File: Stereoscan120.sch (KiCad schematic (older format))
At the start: 0 parts

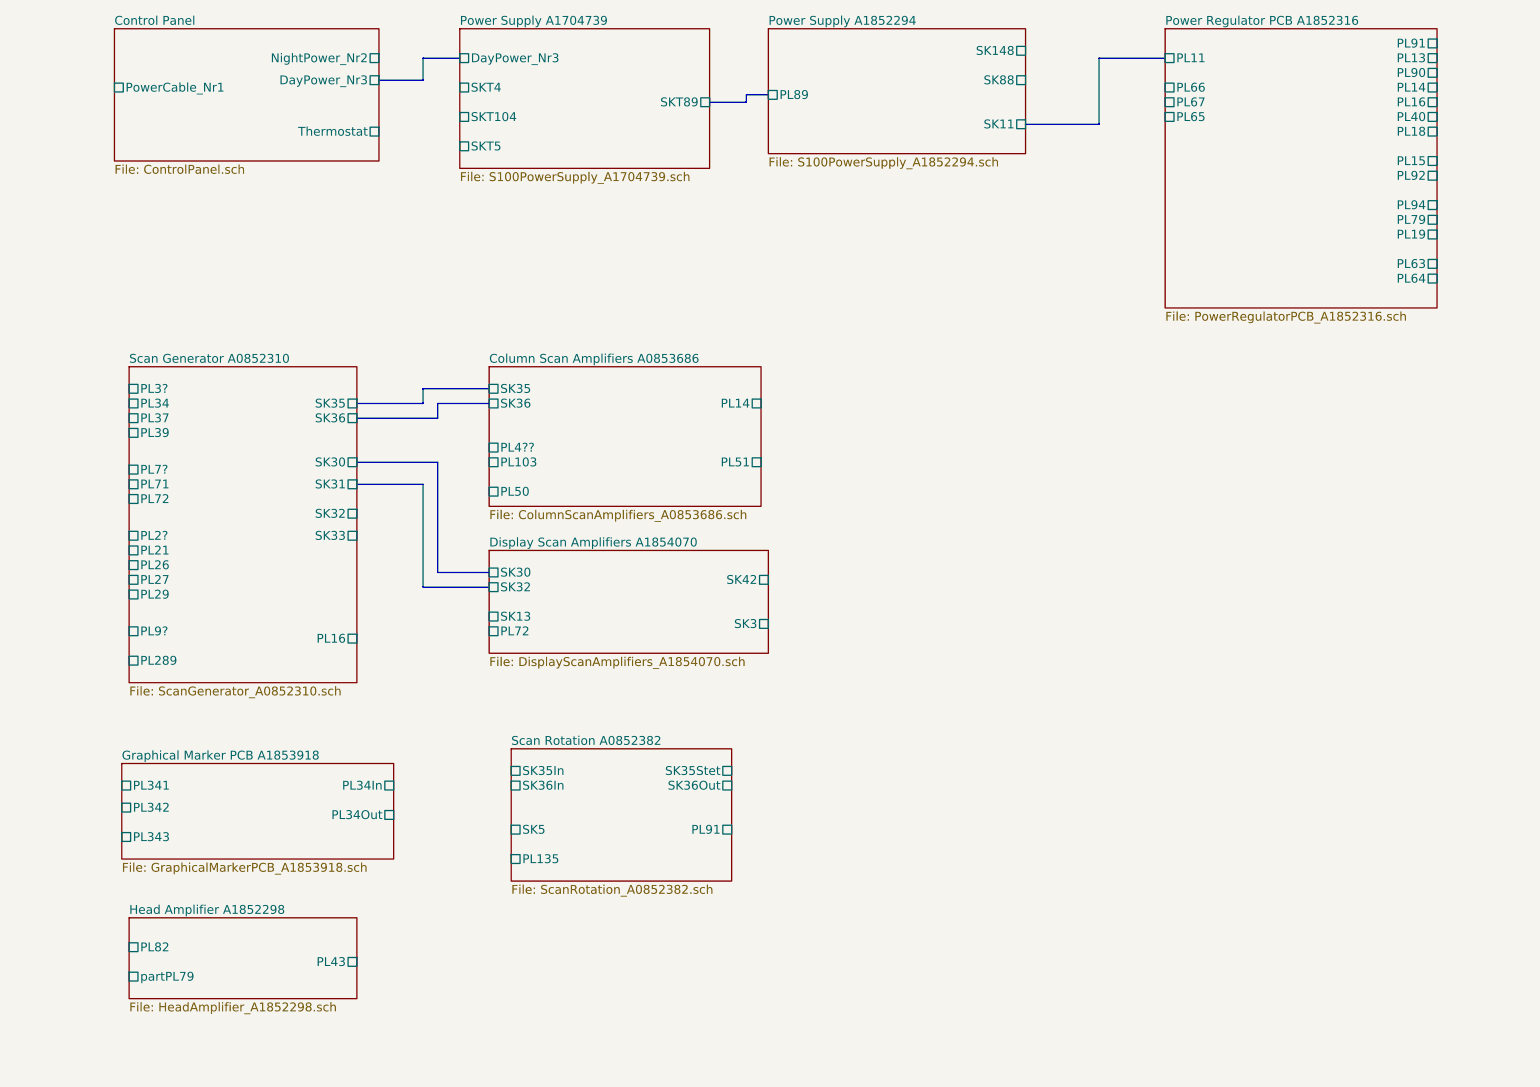
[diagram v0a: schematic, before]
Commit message: Corrects mistakes in existing sub schematics
This corrections were done based on comparison with the actual paper
schematics.
Mainly renaming some pins, which were labled wrongly, plus addid of additional
pins (sockets) which had been overlooked.
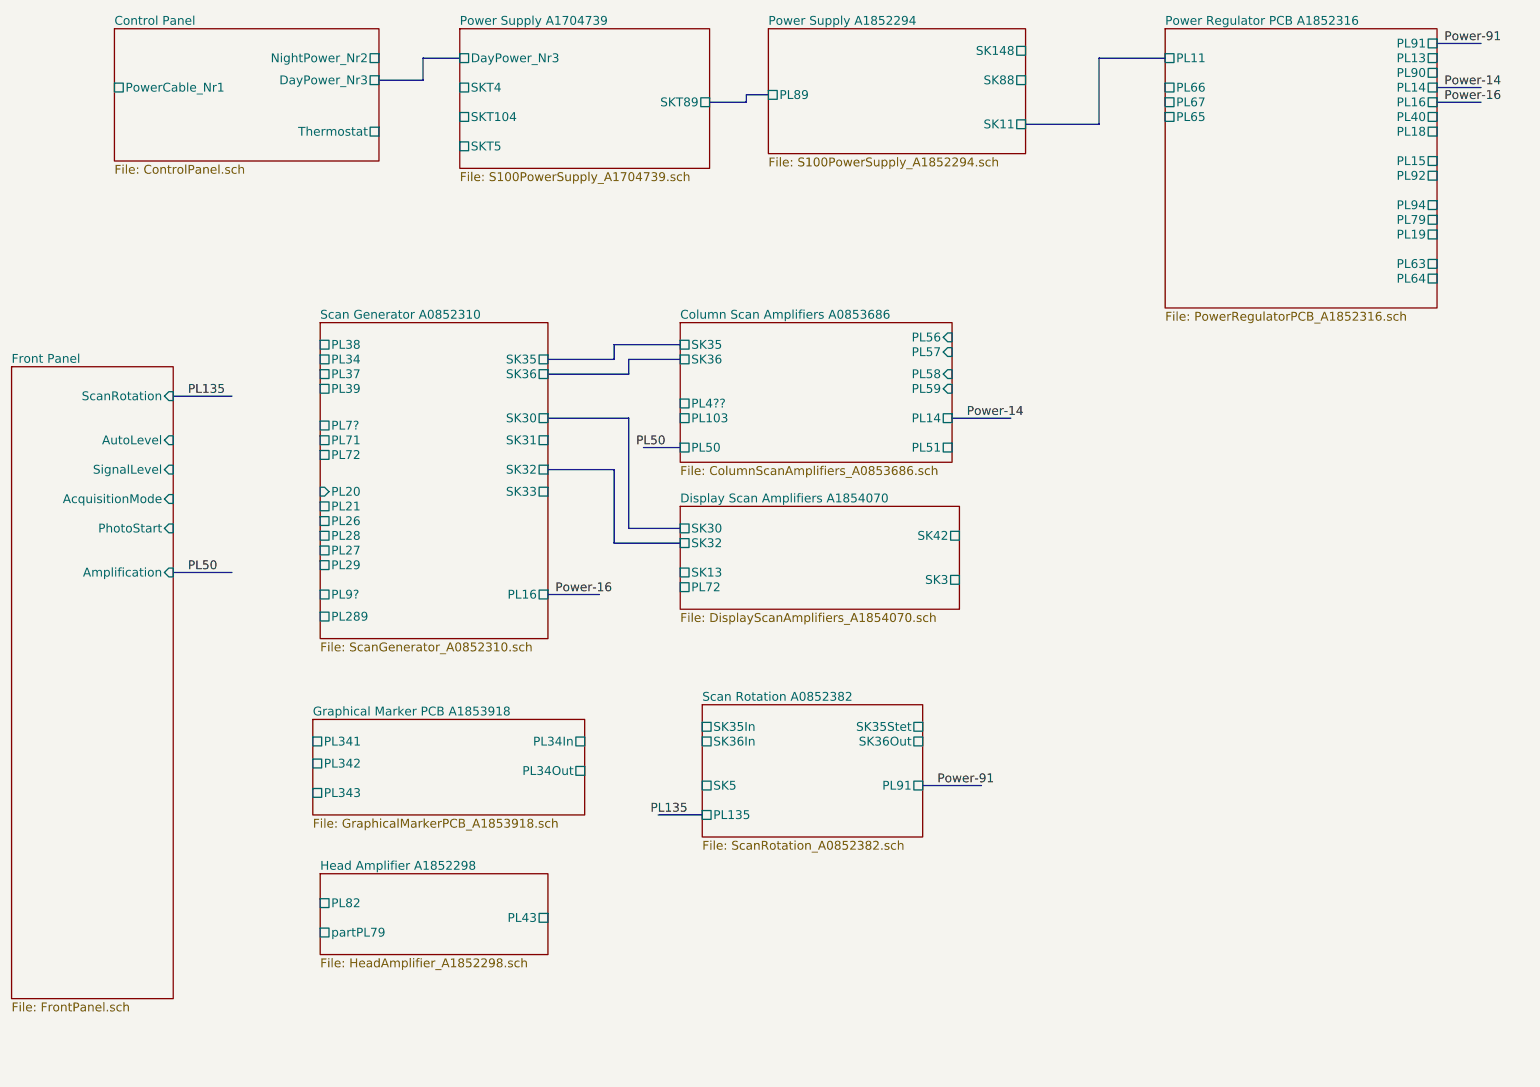
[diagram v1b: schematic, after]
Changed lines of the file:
@@
 LIBS:contrib
 LIBS:valves
+LIBS:Stereoscan120-cache
 EELAYER 26 0
 EELAYER END
-$Descr A4 11693 8268
+$Descr A3 16535 11693
 encoding utf-8
-Sheet 1 11
+Sheet 1 12
 Title ""
 Date ""
@@
 	3500 1000 3750 1000
 $Sheet
-S 3950 3100 1850 950
+S 5250 2800 1850 950
 U 5AAFCB7C
 F0 "Column Scan Amplifiers A0853686" 60
 F1 "ColumnScanAmplifiers_A0853686.sch" 60
-F2 "SK35" U L 3950 3250 60
-F3 "PL50" U L 3950 3950 60
-F4 "PL4??" U L 3950 3650 60
-F5 "PL103" U L 3950 3750 60
-F6 "SK36" U L 3950 3350 60
-F7 "PL51" U R 5800 3750 60
-F8 "PL14" U R 5800 3350 60
-$EndSheet
-$Sheet
-S 1500 3100 1550 2150
+F2 "SK35" U L 5250 2950 60
+F3 "PL50" U L 5250 3650 60
+F4 "PL4??" U L 5250 3350 60
+F5 "PL103" U L 5250 3450 60
+F6 "SK36" U L 5250 3050 60
+F7 "PL51" U R 7100 3650 60
+F8 "PL14" U R 7100 3450 60
+F9 "PL56" I R 7100 2900 60
+F10 "PL57" I R 7100 3000 60
+F11 "PL58" I R 7100 3150 60
+F12 "PL59" I R 7100 3250 60
+$EndSheet
+$Sheet
+S 2800 2800 1550 2150
 U 5AAFE227
 F0 "Scan Generator A0852310" 60
 F1 "ScanGenerator_A0852310.sch" 60
-F2 "PL3?" U L 1500 3250 60
-F3 "PL37" U L 1500 3450 60
-F4 "PL72" U L 1500 4000 60
-F5 "PL2?" U L 1500 4250 60
-F6 "PL27" U L 1500 4550 60
-F7 "PL7?" U L 1500 3800 60
-F8 "PL21" U L 1500 4350 60
-F9 "PL29" U L 1500 4650 60
-F10 "PL39" U L 1500 3550 60
-F11 "SK30" U R 3050 3750 60
-F12 "SK31" U R 3050 3900 60
-F13 "SK36" U R 3050 3450 60
-F14 "SK35" U R 3050 3350 60
-F15 "SK32" U R 3050 4100 60
-F16 "SK33" U R 3050 4250 60
-F17 "PL34" U L 1500 3350 60
-F18 "PL9?" U L 1500 4900 60
-F19 "PL289" U L 1500 5100 60
-F20 "PL71" U L 1500 3900 60
-F21 "PL26" U L 1500 4450 60
-F22 "PL16" U R 3050 4950 60
-$EndSheet
-Wire Bus Line
-	3050 3350 3500 3350
-Wire Bus Line
-	3500 3350 3500 3250
-Wire Bus Line
-	3500 3250 3950 3250
-Wire Bus Line
-	3050 3450 3600 3450
-Wire Bus Line
-	3600 3450 3600 3350
-Wire Bus Line
-	3600 3350 3950 3350
-$Sheet
-S 4100 5700 1500 900
+F2 "PL38" U L 2800 2950 60
+F3 "PL37" U L 2800 3150 60
+F4 "PL72" U L 2800 3700 60
+F5 "PL28" U L 2800 4250 60
+F6 "PL27" U L 2800 4350 60
+F7 "PL7?" U L 2800 3500 60
+F8 "PL21" U L 2800 4050 60
+F9 "PL29" U L 2800 4450 60
+F10 "PL39" U L 2800 3250 60
+F11 "SK30" U R 4350 3450 60
+F12 "SK31" U R 4350 3600 60
+F13 "SK36" U R 4350 3150 60
+F14 "SK35" U R 4350 3050 60
+F15 "SK32" U R 4350 3800 60
+F16 "SK33" U R 4350 3950 60
+F17 "PL34" U L 2800 3050 60
+F18 "PL9?" U L 2800 4650 60
+F19 "PL289" U L 2800 4800 60
+F20 "PL71" U L 2800 3600 60
+F21 "PL26" U L 2800 4150 60
+F22 "PL16" U R 4350 4650 60
+F23 "PL20" I L 2800 3950 60
+$EndSheet
+Wire Bus Line
+	4350 3050 4800 3050
+Wire Bus Line
+	4800 3050 4800 2950
+Wire Bus Line
+	4800 2950 5250 2950
+Wire Bus Line
+	4350 3150 4900 3150
+Wire Bus Line
+	4900 3150 4900 3050
+Wire Bus Line
+	4900 3050 5250 3050
+$Sheet
+S 5400 5400 1500 900
 U 5AB06793
 F0 "Scan Rotation A0852382" 60
 F1 "ScanRotation_A0852382.sch" 60
-F2 "SK35In" U L 4100 5850 60
-F3 "SK36In" U L 4100 5950 60
-F4 "SK5" U L 4100 6250 60
-F5 "PL135" U L 4100 6450 60
-F6 "SK35Stet" U R 5600 5850 60
-F7 "SK36Out" U R 5600 5950 60
-F8 "PL91" U R 5600 6250 60
-$EndSheet
-$Sheet
-S 1450 5800 1850 650
+F2 "SK35In" U L 5400 5550 60
+F3 "SK36In" U L 5400 5650 60
+F4 "SK5" U L 5400 5950 60
+F5 "PL135" U L 5400 6150 60
+F6 "SK35Stet" U R 6900 5550 60
+F7 "SK36Out" U R 6900 5650 60
+F8 "PL91" U R 6900 5950 60
+$EndSheet
+$Sheet
+S 2750 5500 1850 650
 U 5AB087B4
 F0 "Graphical Marker PCB A1853918" 60
 F1 "GraphicalMarkerPCB_A1853918.sch" 60
-F2 "PL341" U L 1450 5950 60
-F3 "PL342" U L 1450 6100 60
-F4 "PL343" U L 1450 6300 60
-F5 "PL34In" U R 3300 5950 60
-F6 "PL34Out" U R 3300 6150 60
-$EndSheet
-$Sheet
-S 1500 6850 1550 550
+F2 "PL341" U L 2750 5650 60
+F3 "PL342" U L 2750 5800 60
+F4 "PL343" U L 2750 6000 60
+F5 "PL34In" U R 4600 5650 60
+F6 "PL34Out" U R 4600 5850 60
+$EndSheet
+$Sheet
+S 2800 6550 1550 550
 U 5AB09F38
 F0 "Head Amplifier A1852298" 60
 F1 "HeadAmplifier_A1852298.sch" 60
-F2 "PL82" U L 1500 7050 60
-F3 "PL43" U R 3050 7150 60
-F4 "partPL79" U L 1500 7250 60
-$EndSheet
-$Sheet
-S 3950 4350 1900 700
+F2 "PL82" U L 2800 6750 60
+F3 "PL43" U R 4350 6850 60
+F4 "partPL79" U L 2800 6950 60
+$EndSheet
+$Sheet
+S 5250 4050 1900 700
 U 5AB0B0A1
 F0 "Display Scan Amplifiers A1854070" 60
 F1 "DisplayScanAmplifiers_A1854070.sch" 60
-F2 "SK30" U L 3950 4500 60
-F3 "SK32" U L 3950 4600 60
-F4 "SK42" U R 5850 4550 60
-F5 "SK3" U R 5850 4850 60
-F6 "SK13" U L 3950 4800 60
-F7 "PL72" U L 3950 4900 60
-$EndSheet
-Wire Bus Line
-	3050 3750 3600 3750
-Wire Bus Line
-	3600 3750 3600 4500
-Wire Bus Line
-	3600 4500 3950 4500
-Wire Bus Line
-	3050 3900 3500 3900
-Wire Bus Line
-	3500 3900 3500 4600
-Wire Bus Line
-	3500 4600 3950 4600
+F2 "SK30" U L 5250 4200 60
+F3 "SK32" U L 5250 4300 60
+F4 "SK42" U R 7150 4250 60
+F5 "SK3" U R 7150 4550 60
+F6 "SK13" U L 5250 4500 60
+F7 "PL72" U L 5250 4600 60
+$EndSheet
+Wire Bus Line
+	4350 3450 4900 3450
+Wire Bus Line
+	4900 3450 4900 4200
+Wire Bus Line
+	4900 4200 5250 4200
+Wire Bus Line
+	4800 4300 5250 4300
+Wire Bus Line
+	4800 4300 4800 3800
+Wire Bus Line
+	4800 3800 4350 3800
+Wire Bus Line
+	4350 4650 4700 4650
+Wire Bus Line
+	7100 3450 7500 3450
+Wire Bus Line
+	10400 900  10700 900
+Wire Bus Line
+	10400 1200 10700 1200
+Wire Bus Line
+	6900 5950 7300 5950
+Wire Bus Line
+	10400 1300 10700 1300
+Text Label 10450 900  0    60   ~ 0
+Power-91
+Text Label 7000 5950 0    60   ~ 0
+Power-91
+Text Label 7200 3450 0    60   ~ 0
+Power-14
+Text Label 10450 1200 0    60   ~ 0
+Power-14
+Text Label 10450 1300 0    60   ~ 0
+Power-16
+Text Label 4400 4650 0    60   ~ 0
+Power-16
+$Sheet
+S 700  3100 1100 4300
+U 5AB959BF
+F0 "Front Panel" 60
+F1 "FrontPanel.sch" 60
+F2 "ScanRotation" I R 1800 3300 60
+F3 "AutoLevel" I R 1800 3600 60
+F4 "SignalLevel" I R 1800 3800 60
+F5 "AcquisitionMode" I R 1800 4000 60
+F6 "PhotoStart" I R 1800 4200 60
+F7 "Amplification" I R 1800 4500 60
+$EndSheet
+Wire Bus Line
+	1800 3300 2200 3300
+Wire Bus Line
+	1800 4500 2200 4500
+Text Label 1900 4500 0    60   ~ 0
+PL50
+Text Label 1900 3300 0    60   ~ 0
+PL135
+Wire Bus Line
+	5250 3650 5000 3650
+Wire Bus Line
+	5400 6150 5100 6150
+Text Label 5300 6150 2    60   ~ 0
+PL135
+Text Label 5150 3650 2    60   ~ 0
+PL50
 $EndSCHEMATC

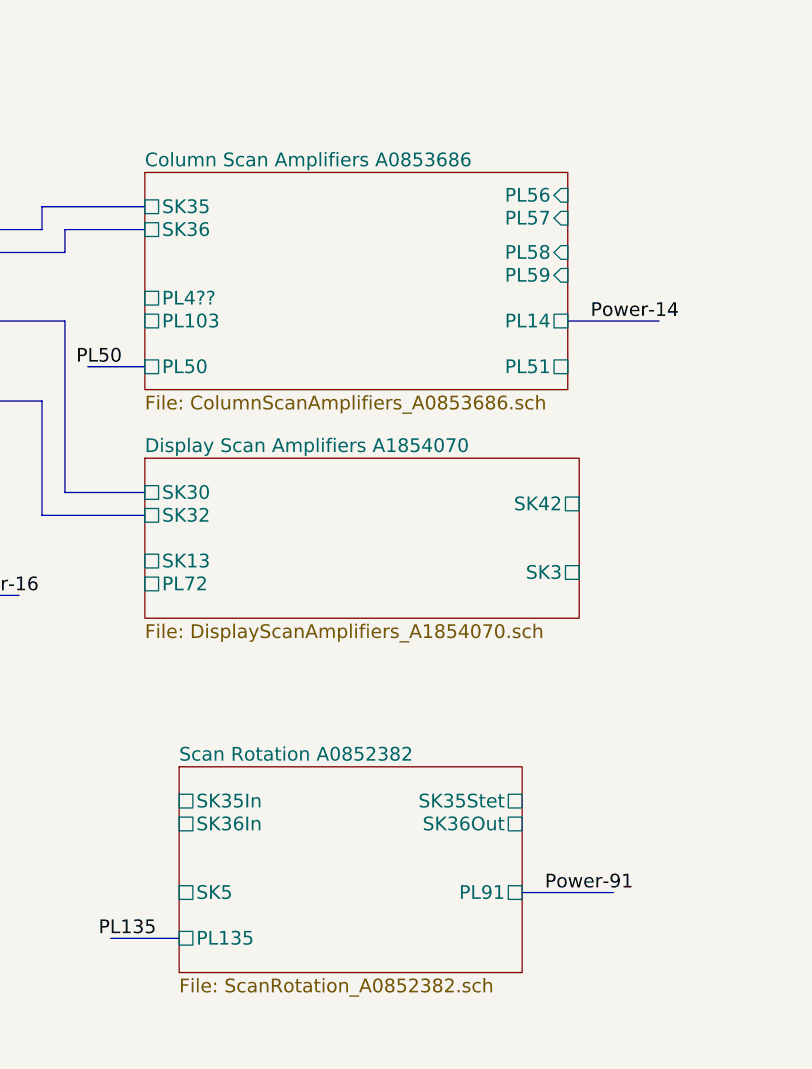
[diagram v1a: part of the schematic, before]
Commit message: Adds Line and Frame deflection inductances
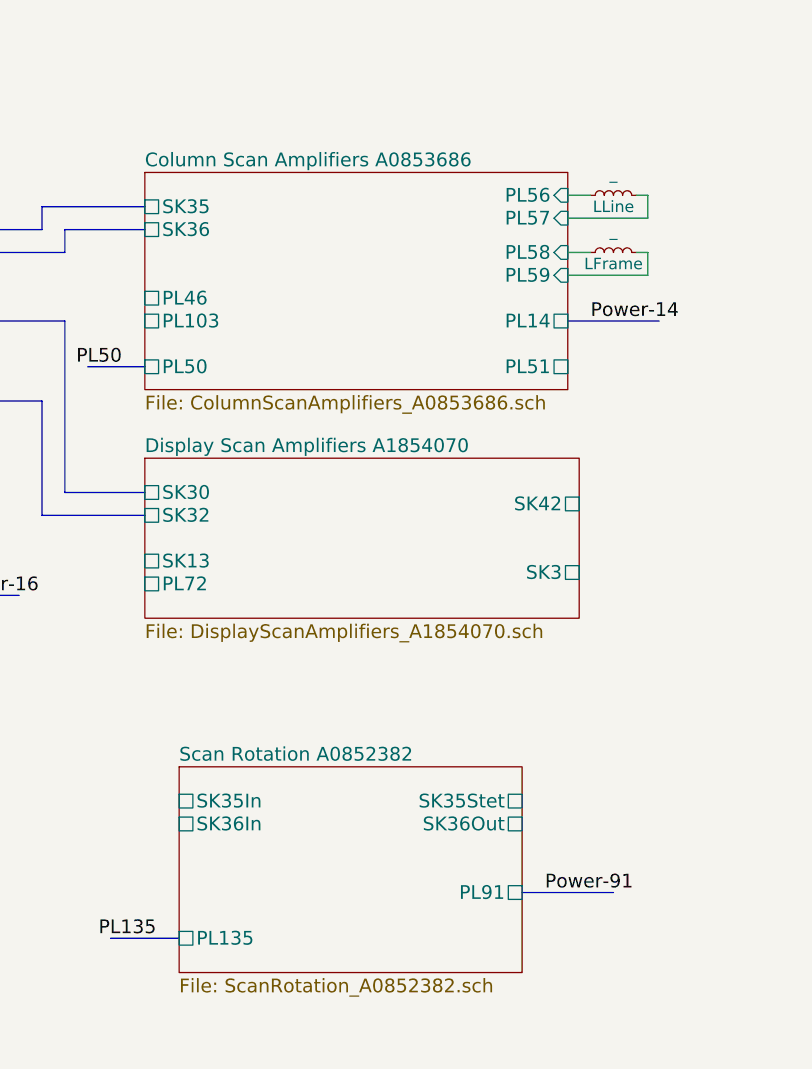
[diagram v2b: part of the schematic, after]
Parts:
- added LFrame, LLine: _, symbol L_Small
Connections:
- net Column Scan Amplifiers A0853686/PL56: now also LLine.1
- net Column Scan Amplifiers A0853686/PL57: now also LLine.2
- net Column Scan Amplifiers A0853686/PL58: now also LFrame.1
- net Column Scan Amplifiers A0853686/PL59: now also LFrame.2
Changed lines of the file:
@@
 F2 "SK35" U L 5250 2950 60
 F3 "PL50" U L 5250 3650 60
-F4 "PL4??" U L 5250 3350 60
+F4 "PL46" U L 5250 3350 60
 F5 "PL103" U L 5250 3450 60
 F6 "SK36" U L 5250 3050 60
@@
 F2 "SK35In" U L 5400 5550 60
 F3 "SK36In" U L 5400 5650 60
-F4 "SK5" U L 5400 5950 60
-F5 "PL135" U L 5400 6150 60
-F6 "SK35Stet" U R 6900 5550 60
-F7 "SK36Out" U R 6900 5650 60
-F8 "PL91" U R 6900 5950 60
+F4 "PL135" U L 5400 6150 60
+F5 "SK35Stet" U R 6900 5550 60
+F6 "SK36Out" U R 6900 5650 60
+F7 "PL91" U R 6900 5950 60
 $EndSheet
 $Sheet
@@
 Text Label 5150 3650 2    60   ~ 0
 PL50
+$Comp
+L L_Small LLine
+U 1 1 5ABA7144
+P 7300 2900
+F 0 "LLine" V 7250 2900 50  0000 C CNN
+F 1 "_" V 7394 2900 50  0000 C CNN
+F 2 "" H 7300 2900 50  0000 C CNN
+F 3 "" H 7300 2900 50  0000 C CNN
+	1    7300 2900
+	0    -1   -1   0
+$EndComp
+$Comp
+L L_Small LFrame
+U 1 1 5ABA7817
+P 7300 3150
+F 0 "LFrame" V 7250 3150 50  0000 C CNN
+F 1 "_" V 7394 3150 50  0000 C CNN
+F 2 "" H 7300 3150 50  0000 C CNN
+F 3 "" H 7300 3150 50  0000 C CNN
+	1    7300 3150
+	0    -1   -1   0
+$EndComp
+Wire Wire Line
+	7200 2900 7100 2900
+Wire Wire Line
+	7400 2900 7450 2900
+Wire Wire Line
+	7450 2900 7450 3000
+Wire Wire Line
+	7450 3000 7100 3000
+Wire Wire Line
+	7100 3150 7200 3150
+Wire Wire Line
+	7400 3150 7450 3150
+Wire Wire Line
+	7450 3150 7450 3250
+Wire Wire Line
+	7450 3250 7100 3250
 $EndSCHEMATC

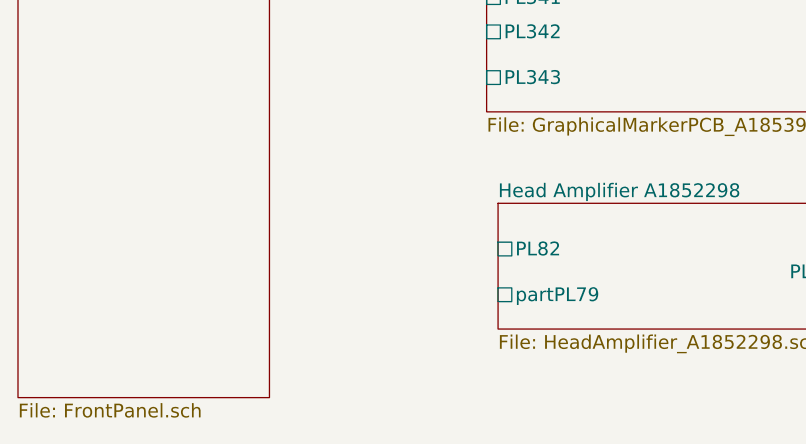
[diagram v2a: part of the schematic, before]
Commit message: Marks part of Plug 79 of Head amplifier as Power
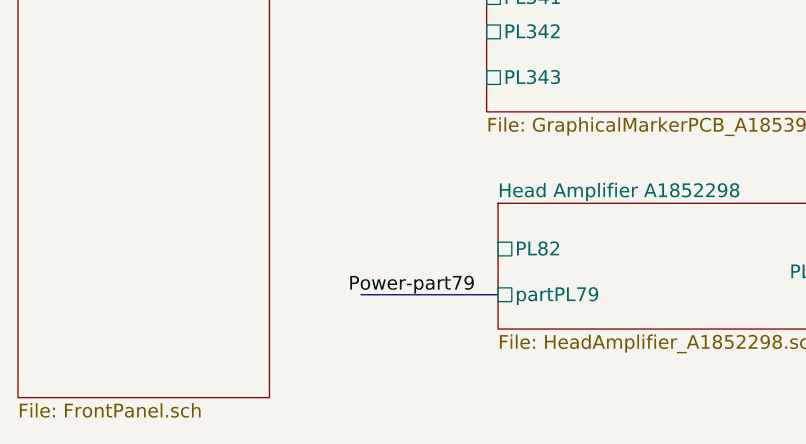
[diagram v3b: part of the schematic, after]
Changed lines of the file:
@@
 Wire Wire Line
 	7450 3250 7100 3250
+Wire Bus Line
+	2800 6950 2200 6950
+Text Label 2700 6950 2    60   ~ 0
+Power-part79
 $EndSCHEMATC
